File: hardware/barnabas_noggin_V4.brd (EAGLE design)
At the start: 100 x 80 mm, 61 parts, among them J1 POWER_JACKPTH, J10 2.54mm, J2 ICSP, J3 ICSP, J4 USB-mini-90 -SMD, J5 ICSP, J6 2.54mm, J7 2.54mm, J8 2.54mm, J9 2.54mm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

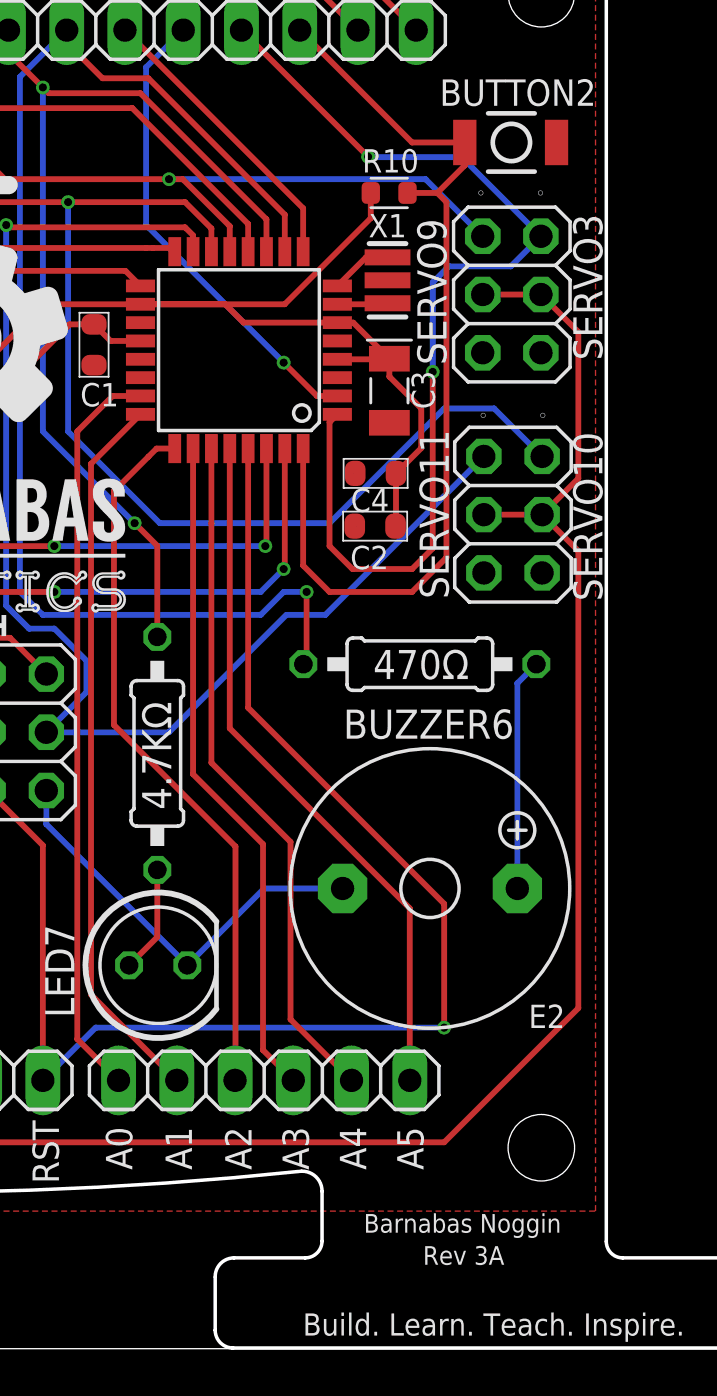
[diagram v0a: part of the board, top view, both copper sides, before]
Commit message: Removed pin2 pullup resistor. Uploaded and updated files for Rev3B.
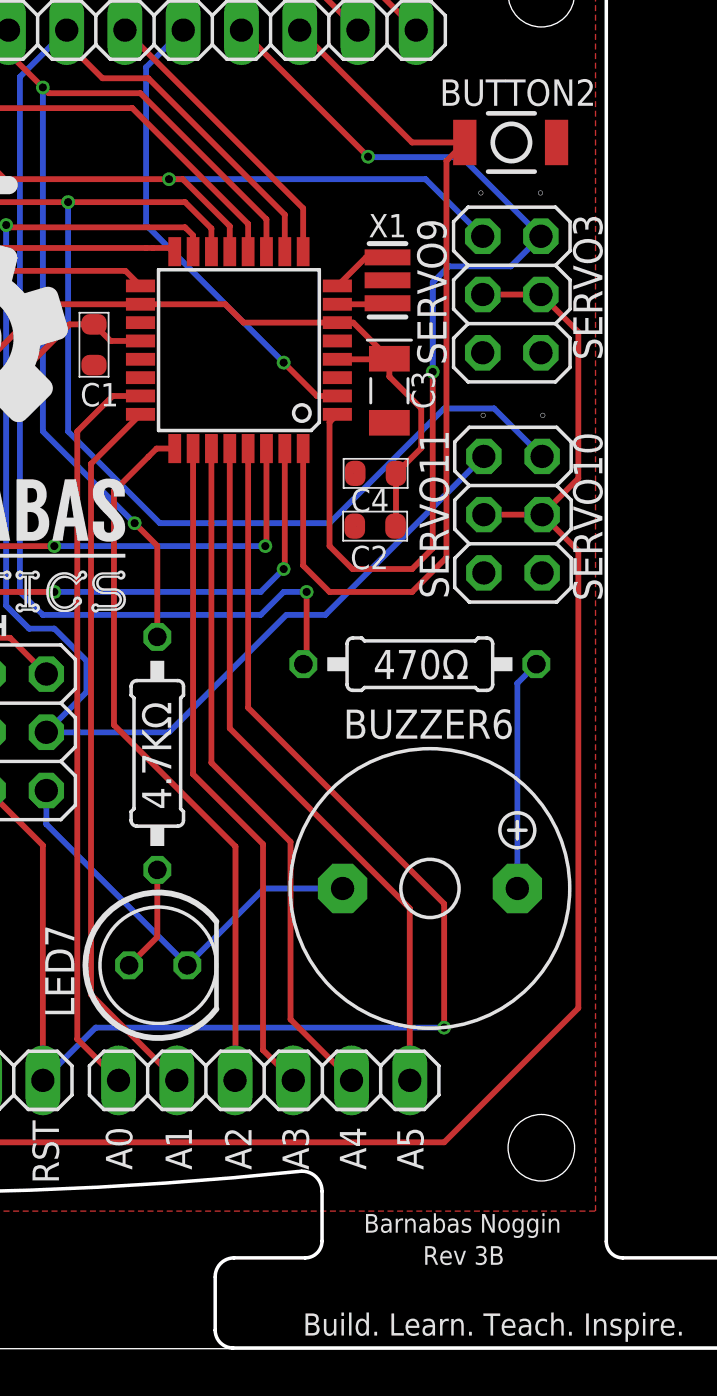
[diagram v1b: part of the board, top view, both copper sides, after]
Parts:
- removed R10: 1K, barnabas_noggin_V4:R0603
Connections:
- net 5V: no longer R10.2
- net D2: no longer R10.1
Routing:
- net 5V: track 135.7 -> 123.0 mm
- net D2: track 41.7 -> 40.1 mm
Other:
- board text added: "Rev 3B"
- board text removed: "Rev 3A"

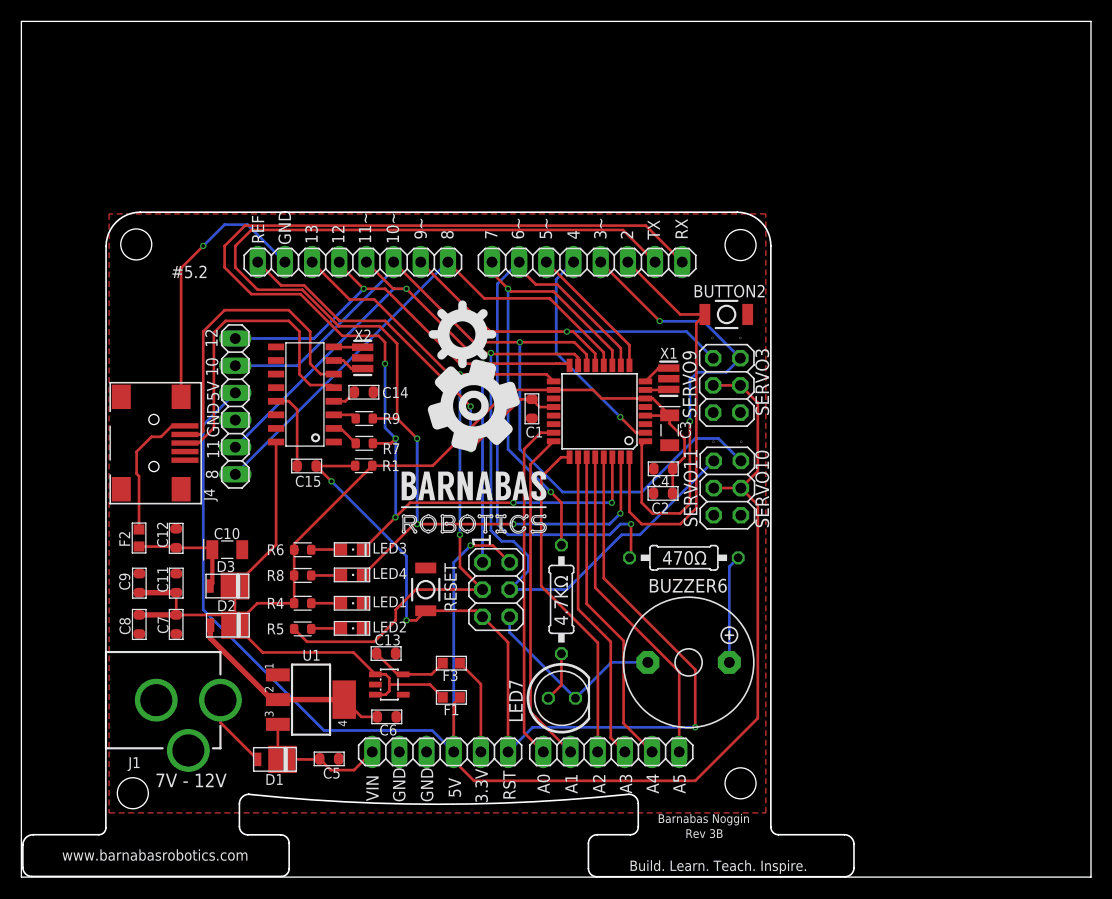
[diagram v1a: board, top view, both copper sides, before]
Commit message: Update library for V4 board
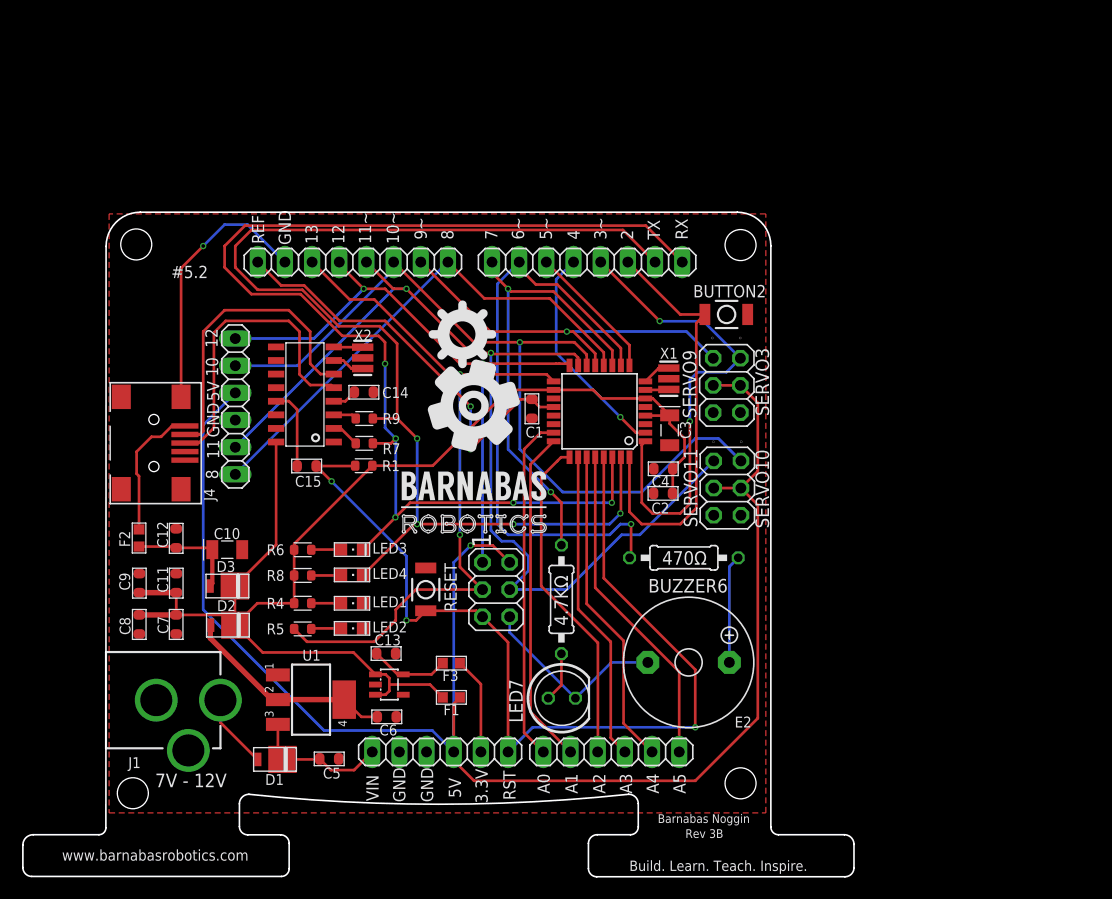
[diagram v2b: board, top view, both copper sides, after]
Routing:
- net VIN: track 14.0 -> 13.0 mm
- net D9: track 36.2 -> 35.7 mm
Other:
- board size 100 x 80 mm -> 77.7 x 62.1 mm
